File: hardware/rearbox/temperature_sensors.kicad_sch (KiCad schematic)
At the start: 0 parts

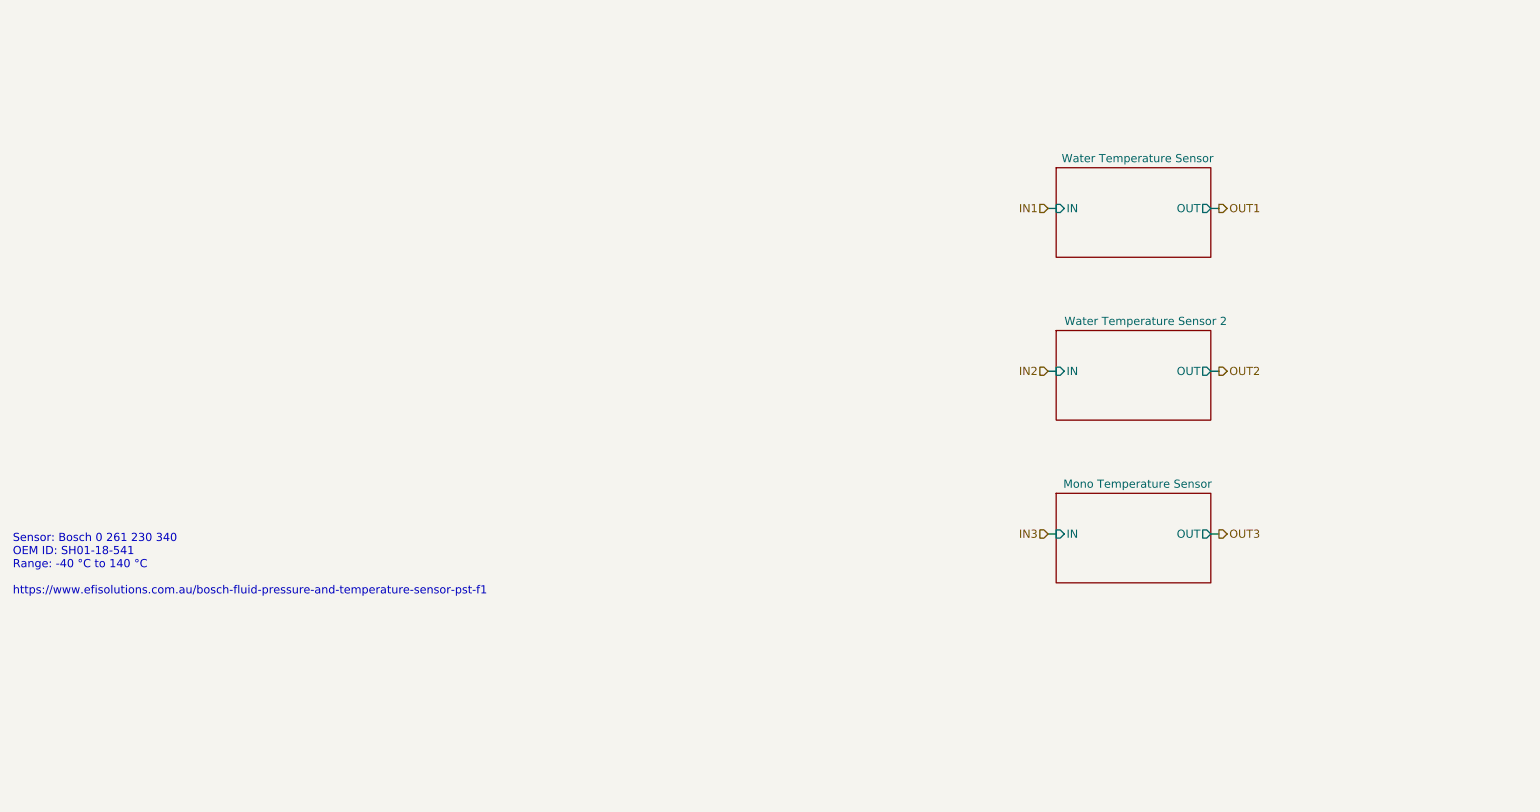
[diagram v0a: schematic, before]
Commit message: Place components on the PCB
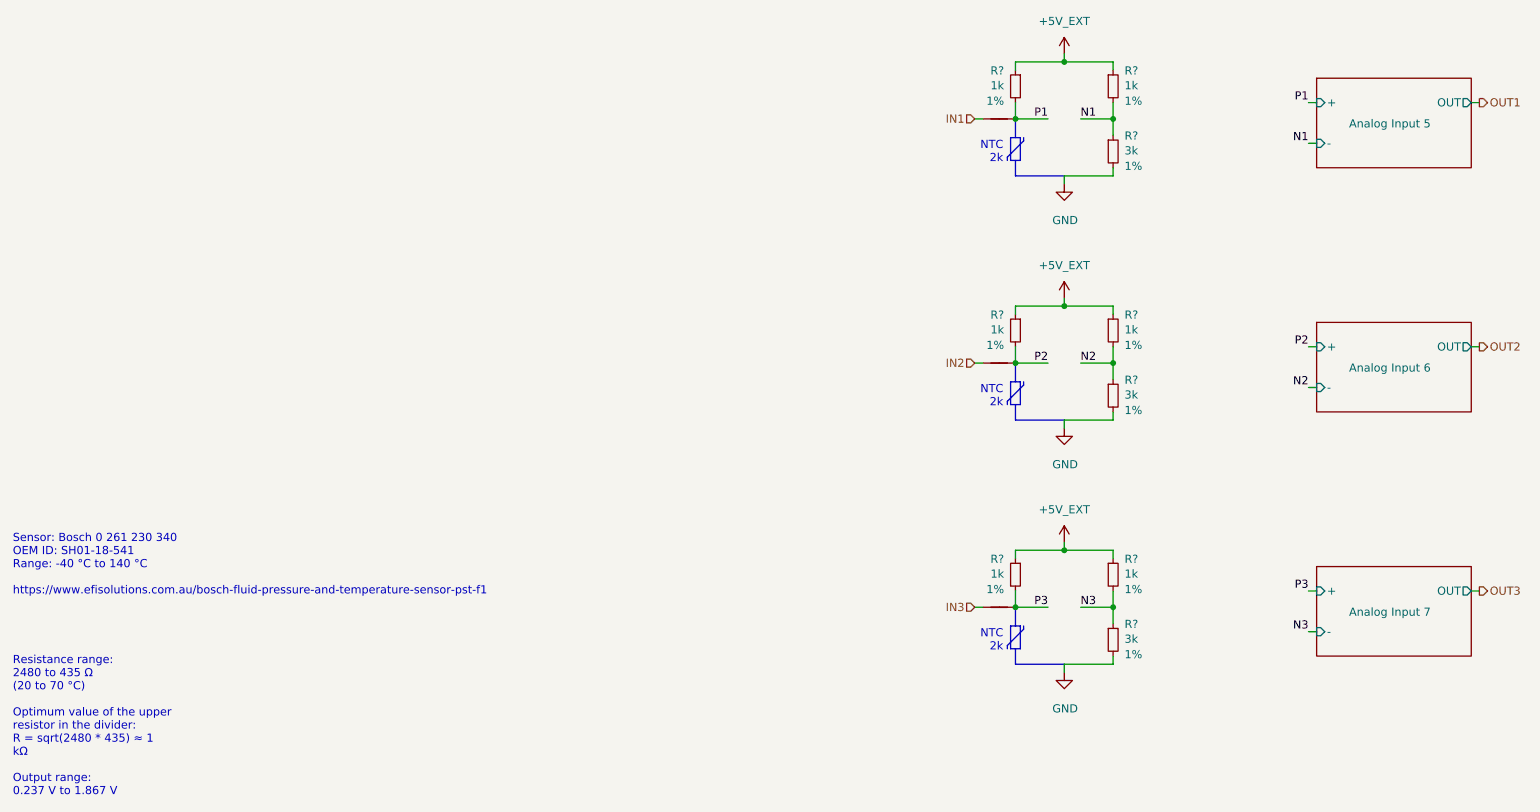
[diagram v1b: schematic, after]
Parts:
- added NT5, NT6, NT7: NetTie_2, NetTie:NetTie-2_SMD_Pad0.5mm, symbol Device:NetTie_2
- added R? (x6): 1k, Resistor_SMD:R_0603_1608Metric, symbol Device:R_Small
- added R? (x3): 3k, Resistor_SMD:R_0603_1608Metric, symbol Device:R_Small
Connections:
- net IN1: now also NT5.1
- net IN2: now also NT6.1
- net IN3: now also NT7.1
- new net +5V_EXT: R?.1, R?.1, R?.1, R?.1, R?.1, R?.1
- new net GND: R?.2, R?.2, R?.2
- new net N1: R?.1, R?.2
- new net N2: R?.1, R?.2
- new net N3: R?.1, R?.2
- new net P1: NT5.2, R?.2
- new net P2: NT6.2, R?.2
- new net P3: NT7.2, R?.2
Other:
- removed sheet Mono Temperature Sensor
- removed sheet Water Temperature Sensor
- removed sheet Water Temperature Sensor 2
- added sheet Analog Input 5 (analog_input.kicad_sch)
- added sheet Analog Input 6 (analog_input.kicad_sch)
- added sheet Analog Input 7 (analog_input.kicad_sch)
- note added: "NTC 2k"

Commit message: Fix DRCs
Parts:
- NT5, NT6, NT7: footprint NetTie:NetTie-2_SMD_Pad0.5mm -> Local_Library:NetTie-2_SMD_Pad0.2mm
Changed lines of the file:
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@@
   (title_block
     (title "Temperature Sensors")
-    (date "2023-11-02")
+    (date "2023-11-17")
     (rev "${REVISION}")
     (company "Author: I. Kajdan")
@@
       (effects (font (size 1.27 1.27)) hide)
     )
-    (property "Footprint" "NetTie:NetTie-2_SMD_Pad0.5mm" (at 177.8 128.27 0)
+    (property "Footprint" "Local_Library:NetTie-2_SMD_Pad0.2mm" (at 177.8 128.27 0)
       (effects (font (size 1.27 1.27)) hide)
     )
@@
       (effects (font (size 1.27 1.27)) hide)
     )
-    (property "Footprint" "NetTie:NetTie-2_SMD_Pad0.5mm" (at 177.8 90.17 0)
+    (property "Footprint" "Local_Library:NetTie-2_SMD_Pad0.2mm" (at 177.8 90.17 0)
       (effects (font (size 1.27 1.27)) hide)
     )
@@
       (effects (font (size 1.27 1.27)) hide)
     )
-    (property "Footprint" "NetTie:NetTie-2_SMD_Pad0.5mm" (at 177.8 52.07 0)
+    (property "Footprint" "Local_Library:NetTie-2_SMD_Pad0.2mm" (at 177.8 52.07 0)
       (effects (font (size 1.27 1.27)) hide)
     )

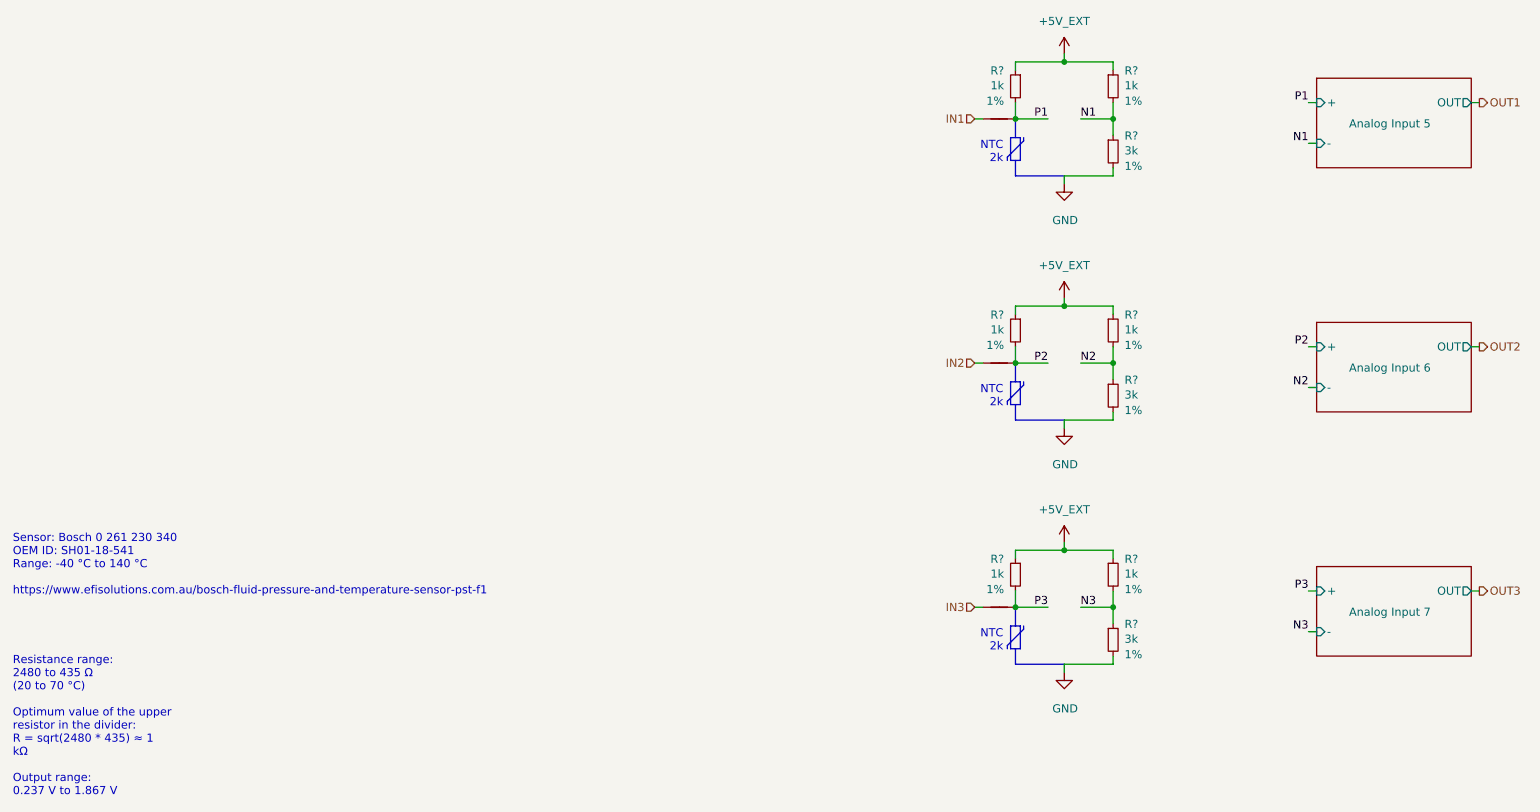
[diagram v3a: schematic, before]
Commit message: Route the tracks on the connector PCB
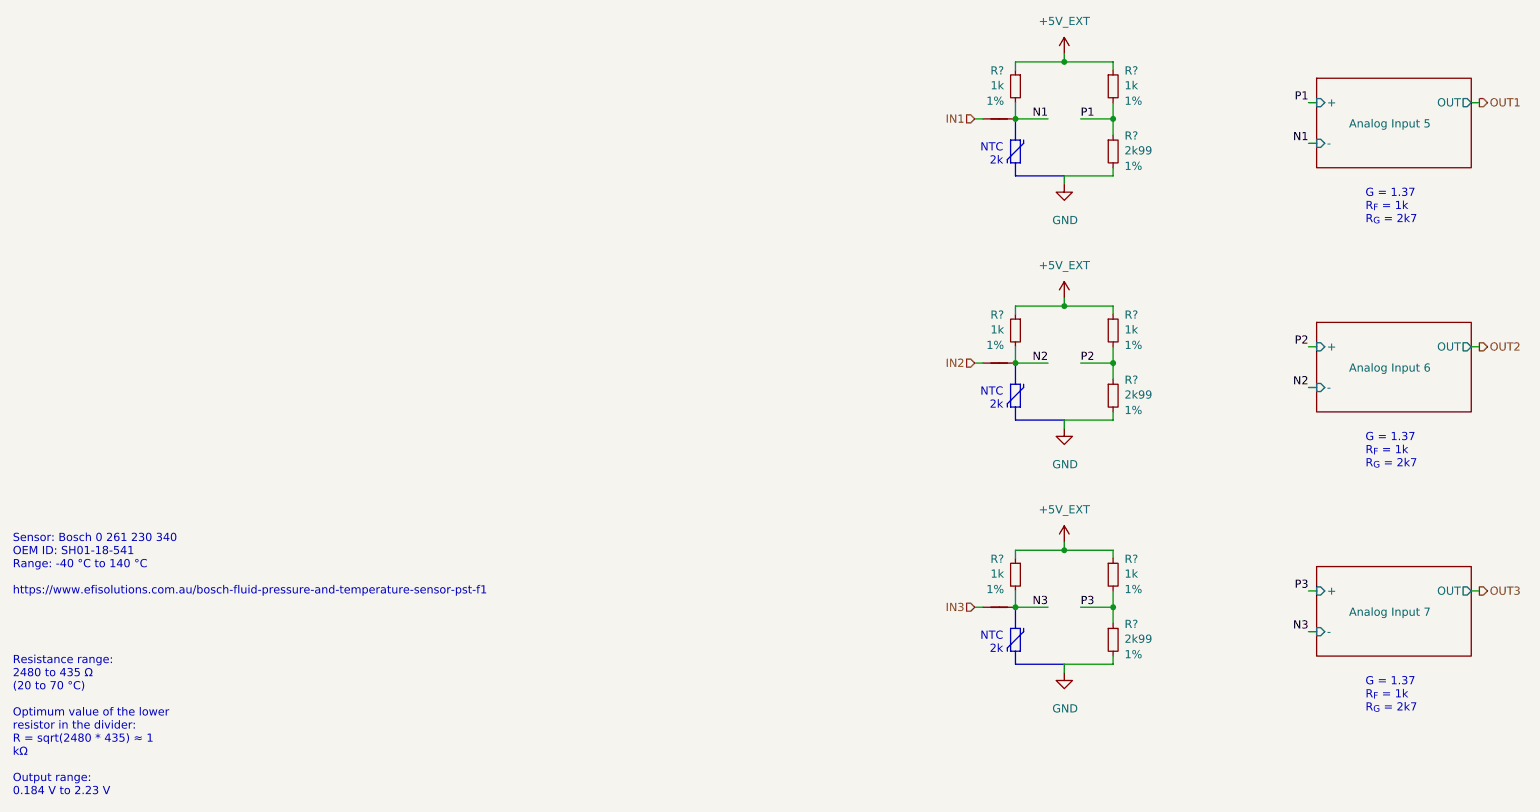
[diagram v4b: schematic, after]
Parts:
- R? (x3): value 3k -> 2k99
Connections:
- net N1: now also NT5.2, R?.2; no longer R?.1, R?.2
- net N2: now also NT6.2, R?.2; no longer R?.1, R?.2
- net N3: now also NT7.2, R?.2; no longer R?.1, R?.2
- net P1: now also R?.1, R?.2; no longer NT5.2, R?.2
- net P2: now also R?.1, R?.2; no longer NT6.2, R?.2
- net P3: now also R?.1, R?.2; no longer NT7.2, R?.2
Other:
- note added: "G = 1.37 R_{F} = 1k R_{G} = 2k7"

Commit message: Fix measurement bridges polarity
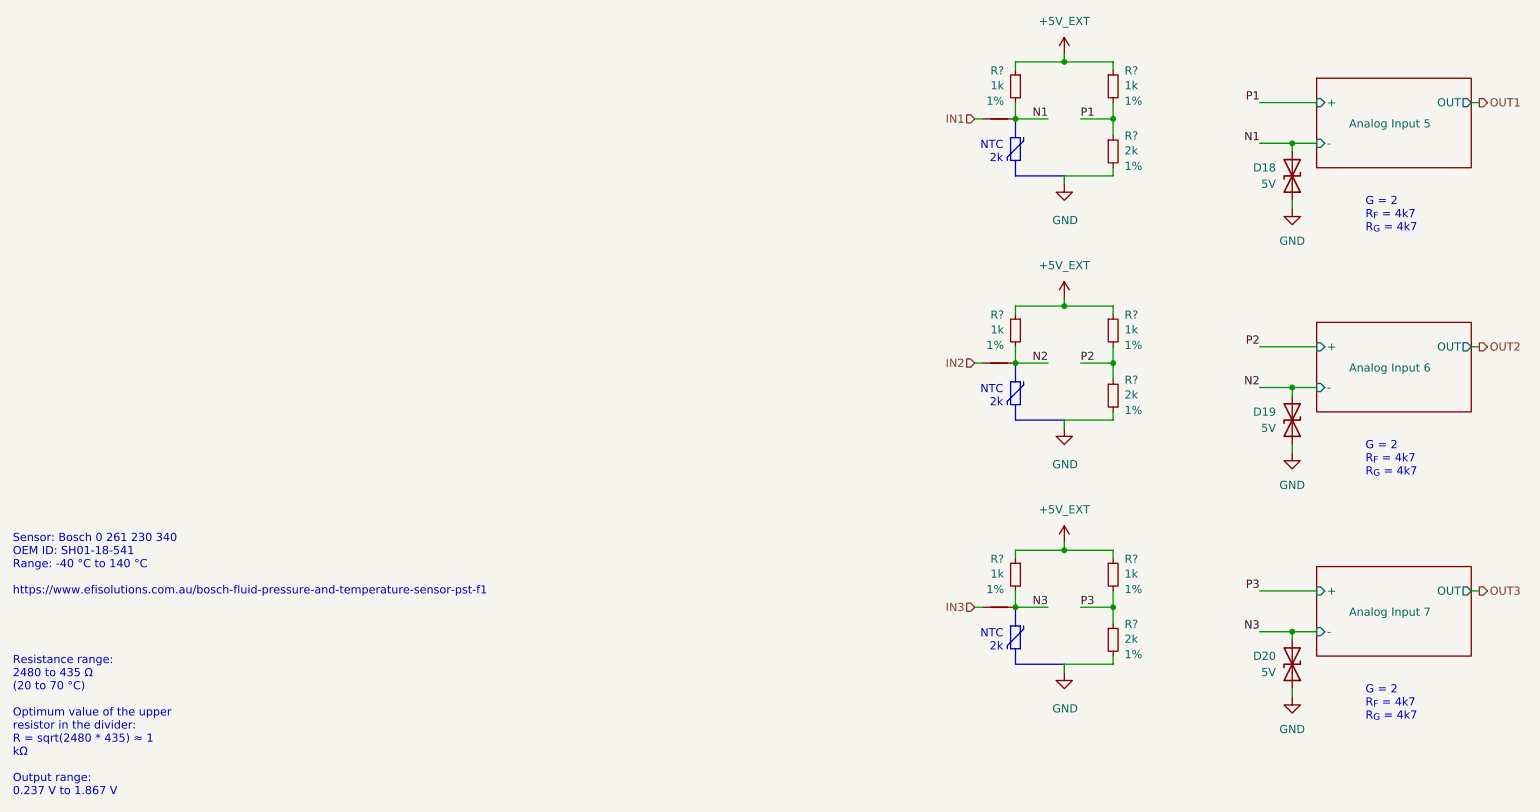
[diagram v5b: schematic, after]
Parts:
- added D18, D19, D20: 5V, Diode_SMD:D_SOD-523, symbol Device:D_TVS
- R? (x3): value 2k99 -> 2k
- renumbered NT5 to NT1, NT6 to NT2, NT7 to NT3
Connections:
- net GND: now also D18.1 (A1), D19.1 (A1), D20.1 (A1)
- net N1: now also D18.2 (A2)
- net N2: now also D19.2 (A2)
- net N3: now also D20.2 (A2)
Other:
- note added: "G = 2 R_{F} = 4k7 R_{G} = 4k7"
- note removed: "G = 1.37 R_{F} = 1k R_{G} = 2k7"
